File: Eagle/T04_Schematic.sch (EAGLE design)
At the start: 30 parts

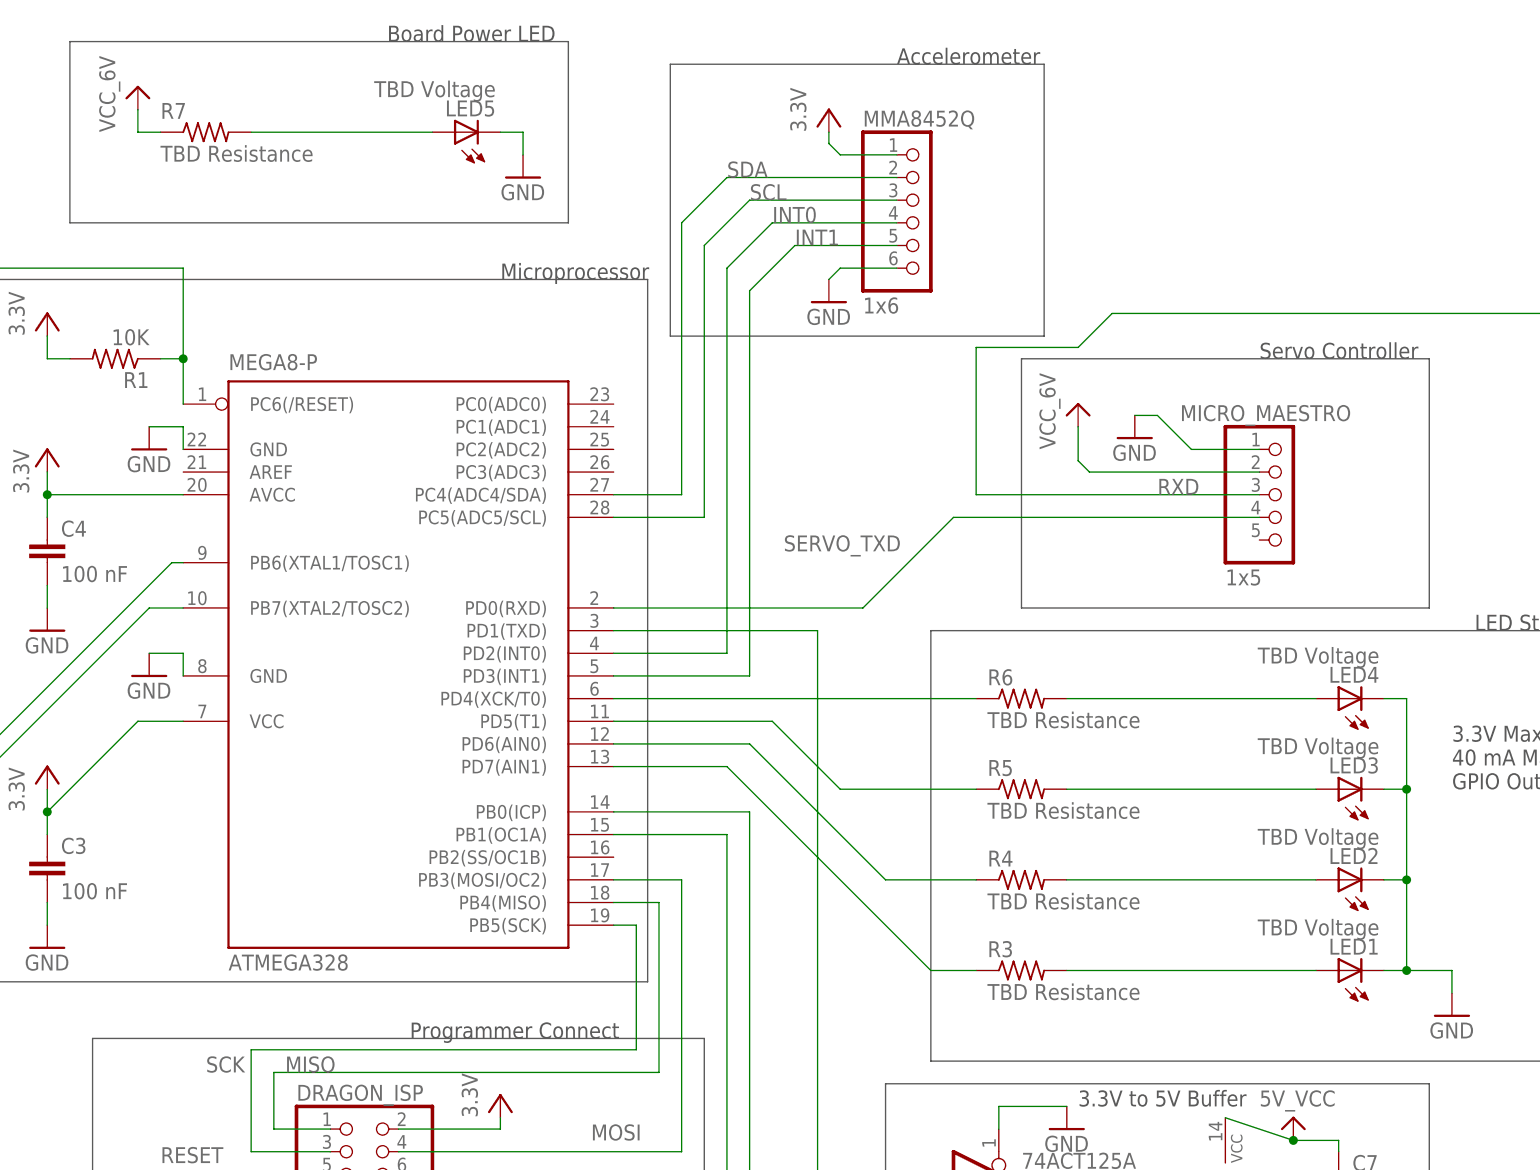
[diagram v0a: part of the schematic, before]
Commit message: Added Resistor and LED Voltages
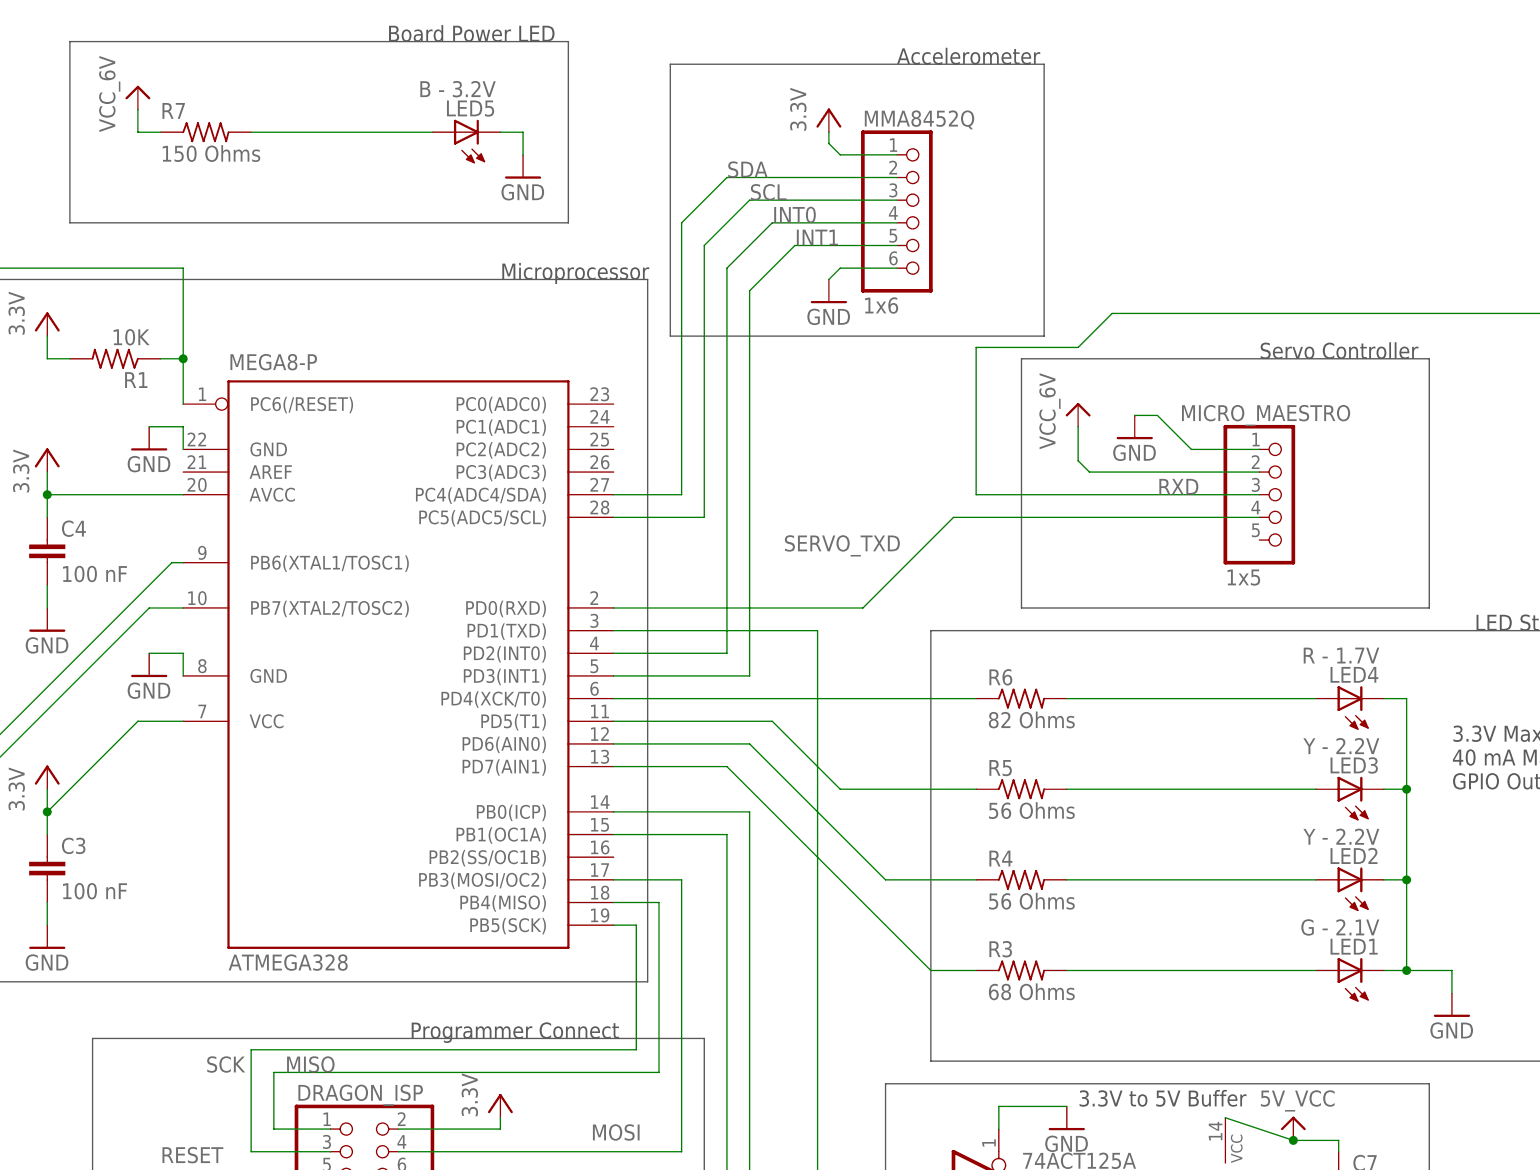
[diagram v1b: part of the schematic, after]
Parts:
- LED1: value TBD Voltage -> G - 2.1V
- LED2, LED3: value TBD Voltage -> Y - 2.2V
- LED4: value TBD Voltage -> R - 1.7V
- LED5: value TBD Voltage -> B - 3.2V
- R3: value TBD Resistance -> 68 Ohms
- R4, R5: value TBD Resistance -> 56 Ohms
- R6: value TBD Resistance -> 82 Ohms
- R7: value TBD Resistance -> 150 Ohms
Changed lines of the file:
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@@
 <part name="C4" library="rcl" deviceset="C-EU" device="C1206" value="100 nF"/>
 <part name="C3" library="rcl" deviceset="C-EU" device="C1206" value="100 nF"/>
-<part name="LED1" library="led" deviceset="LED" device="SMT1206" value="TBD Voltage"/>
-<part name="LED2" library="led" deviceset="LED" device="SMT1206" value="TBD Voltage"/>
-<part name="LED3" library="led" deviceset="LED" device="SMT1206" value="TBD Voltage"/>
-<part name="LED4" library="led" deviceset="LED" device="SMT1206" value="TBD Voltage"/>
-<part name="R3" library="rcl" deviceset="R-US_" device="R1206" value="TBD Resistance"/>
-<part name="R4" library="rcl" deviceset="R-US_" device="R1206" value="TBD Resistance"/>
-<part name="R5" library="rcl" deviceset="R-US_" device="R1206" value="TBD Resistance"/>
-<part name="R6" library="rcl" deviceset="R-US_" device="R1206" value="TBD Resistance"/>
+<part name="LED1" library="led" deviceset="LED" device="SMT1206" value="G - 2.1V"/>
+<part name="LED2" library="led" deviceset="LED" device="SMT1206" value="Y - 2.2V"/>
+<part name="LED3" library="led" deviceset="LED" device="SMT1206" value="Y - 2.2V"/>
+<part name="LED4" library="led" deviceset="LED" device="SMT1206" value="R - 1.7V"/>
+<part name="R3" library="rcl" deviceset="R-US_" device="R1206" value="68 Ohms"/>
+<part name="R4" library="rcl" deviceset="R-US_" device="R1206" value="56 Ohms"/>
+<part name="R5" library="rcl" deviceset="R-US_" device="R1206" value="56 Ohms"/>
+<part name="R6" library="rcl" deviceset="R-US_" device="R1206" value="82 Ohms"/>
 <part name="GND11" library="supply1" deviceset="GND" device=""/>
 <part name="VCC_6V_1" library="Taylor_Griffin_T04" deviceset="VCC_6V" device=""/>
@@
 <part name="VCC_6V_5" library="Taylor_Griffin_T04" deviceset="VCC_6V" device=""/>
 <part name="GND12" library="supply1" deviceset="GND" device=""/>
-<part name="R7" library="rcl" deviceset="R-US_" device="R1206" value="TBD Resistance"/>
-<part name="LED5" library="led" deviceset="LED" device="SMT1206" value="TBD Voltage"/>
+<part name="R7" library="rcl" deviceset="R-US_" device="R1206" value="150 Ohms"/>
+<part name="LED5" library="led" deviceset="LED" device="SMT1206" value="B - 3.2V"/>
 <part name="OSC1" library="SparkFun-FreqCtrl" deviceset="CRYSTAL" device="HC49US" value="16 MHz"/>
 <part name="C1" library="rcl" deviceset="C-EU" device="C1206" value="22pF"/>
